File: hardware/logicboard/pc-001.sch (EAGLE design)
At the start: 17 parts, among them J4 DNP, J5 DNP

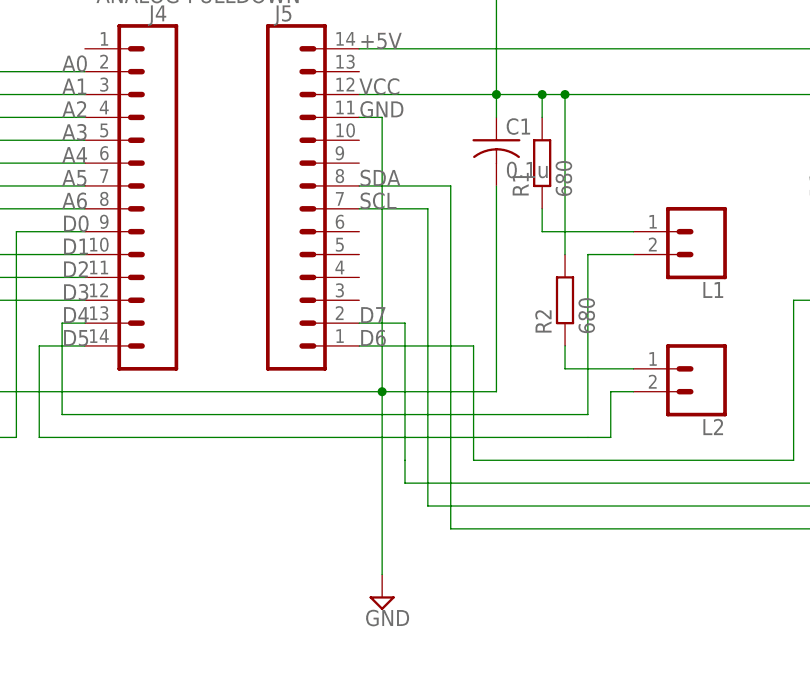
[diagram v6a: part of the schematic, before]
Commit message: Fixed connection of SDA.
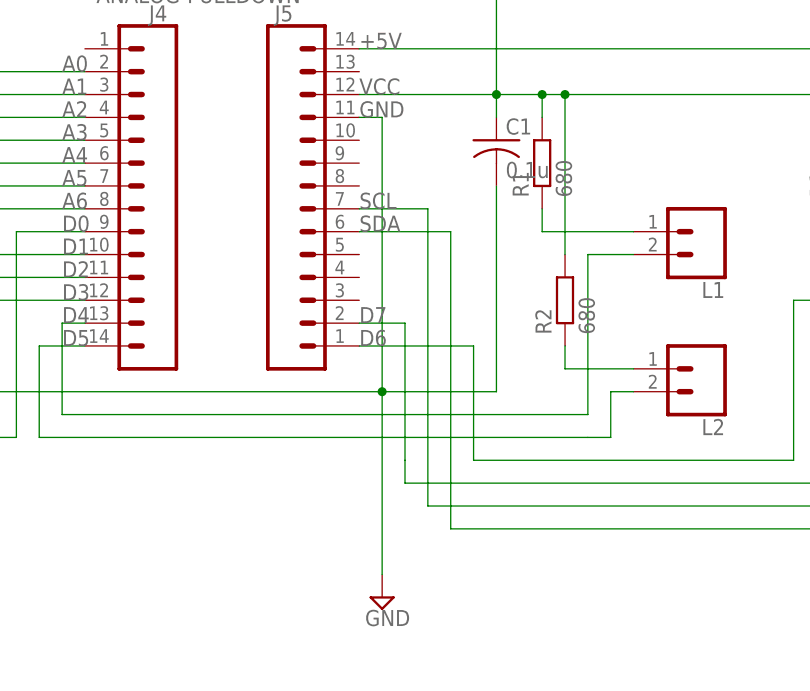
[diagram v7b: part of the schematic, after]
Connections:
- net SDA: now also J5.6; no longer J5.8
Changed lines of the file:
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@@
 <net name="SDA" class="0">
 <segment>
-<pinref part="J5" gate="G$1" pin="8"/>
-<wire x1="119.38" y1="93.98" x2="129.54" y2="93.98" width="0.1524" layer="91"/>
-<wire x1="129.54" y1="93.98" x2="129.54" y2="55.88" width="0.1524" layer="91"/>
 <pinref part="I2C" gate="G$1" pin="4"/>
 <wire x1="129.54" y1="55.88" x2="172.72" y2="55.88" width="0.1524" layer="91"/>
@@
 <junction x="172.72" y="88.9"/>
 <label x="177.8" y="88.9" size="1.778" layer="95"/>
-<label x="119.38" y="93.98" size="1.778" layer="95"/>
+<wire x1="129.54" y1="55.88" x2="129.54" y2="88.9" width="0.1524" layer="91"/>
+<pinref part="J5" gate="G$1" pin="6"/>
+<wire x1="129.54" y1="88.9" x2="119.38" y2="88.9" width="0.1524" layer="91"/>
+<label x="119.38" y="88.9" size="1.778" layer="95"/>
 </segment>
 </net>
